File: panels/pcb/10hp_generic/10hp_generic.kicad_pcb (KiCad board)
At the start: 2 copper layers, 49.9 x 109.2 mm, 81 parts, among them J1 Conn_02x04_Odd_Even, J2 SWD, SW1 SW_Push, SW10 SW_Push, SW11 SW_Push, SW12 SW_Push, SW13 SW_Push, SW14 SW_Push, SW15 SW_Push, SW16 SW_Push, SW2 SW_Push, SW3 SW_Push, SW4 SW_Push, SW5 SW_Push, SW6 SW_Push, SW7 SW_Push, SW8 SW_Push, SW9 SW_Push, U1 STM32F072RBTx, U2 AMS1117-3.3

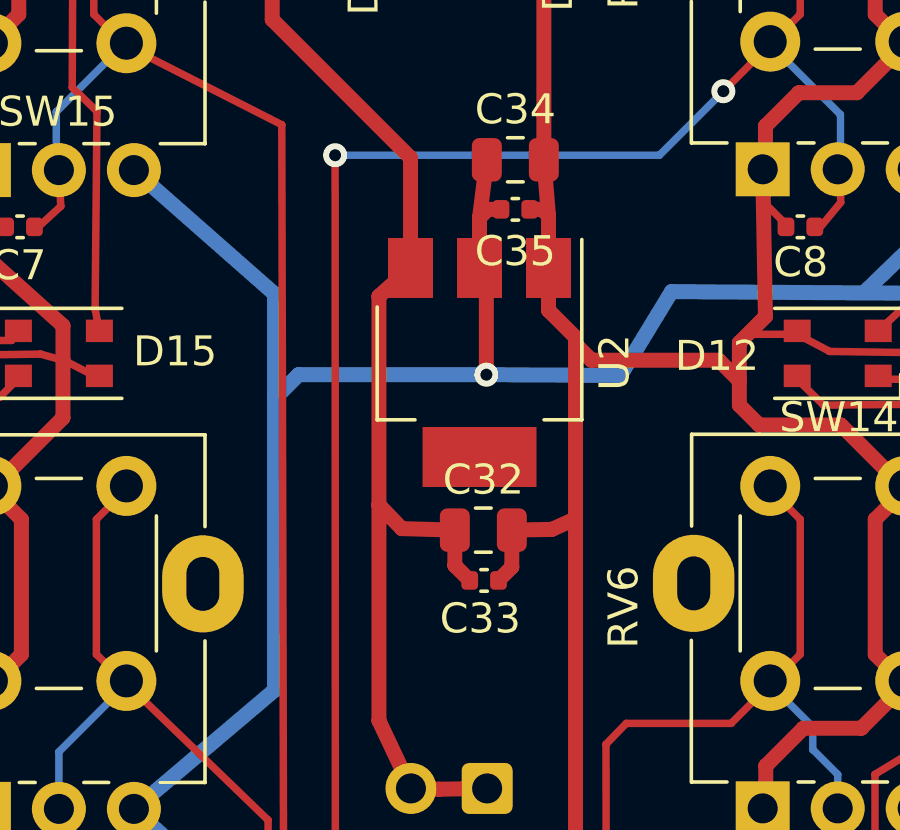
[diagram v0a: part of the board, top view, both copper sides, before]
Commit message: Fixes some component values
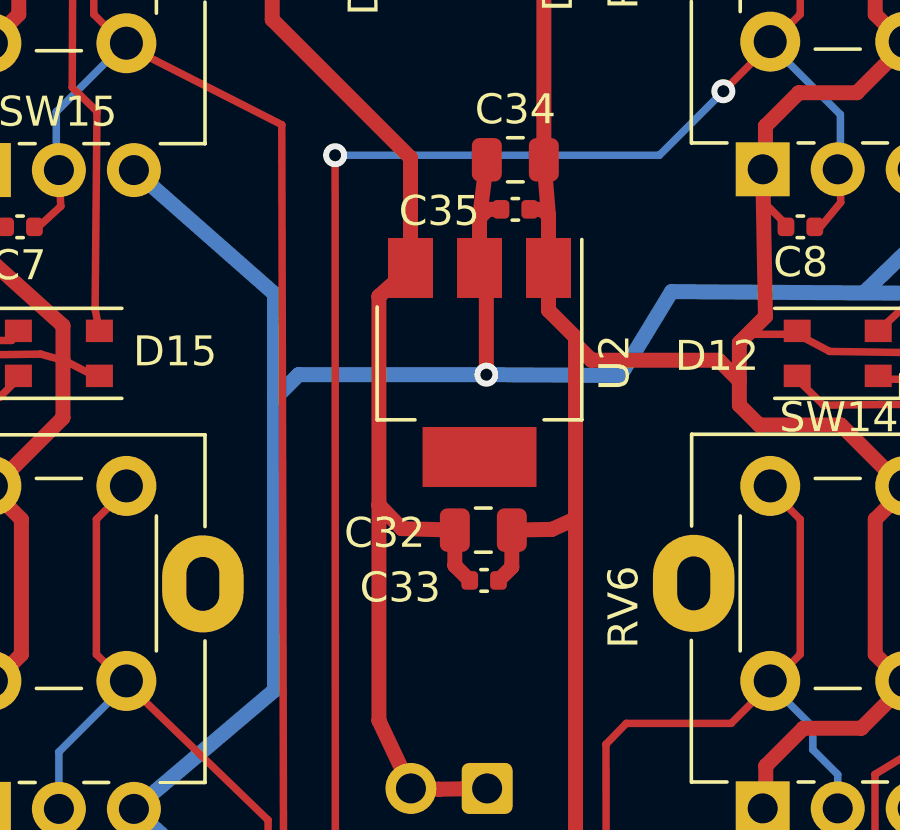
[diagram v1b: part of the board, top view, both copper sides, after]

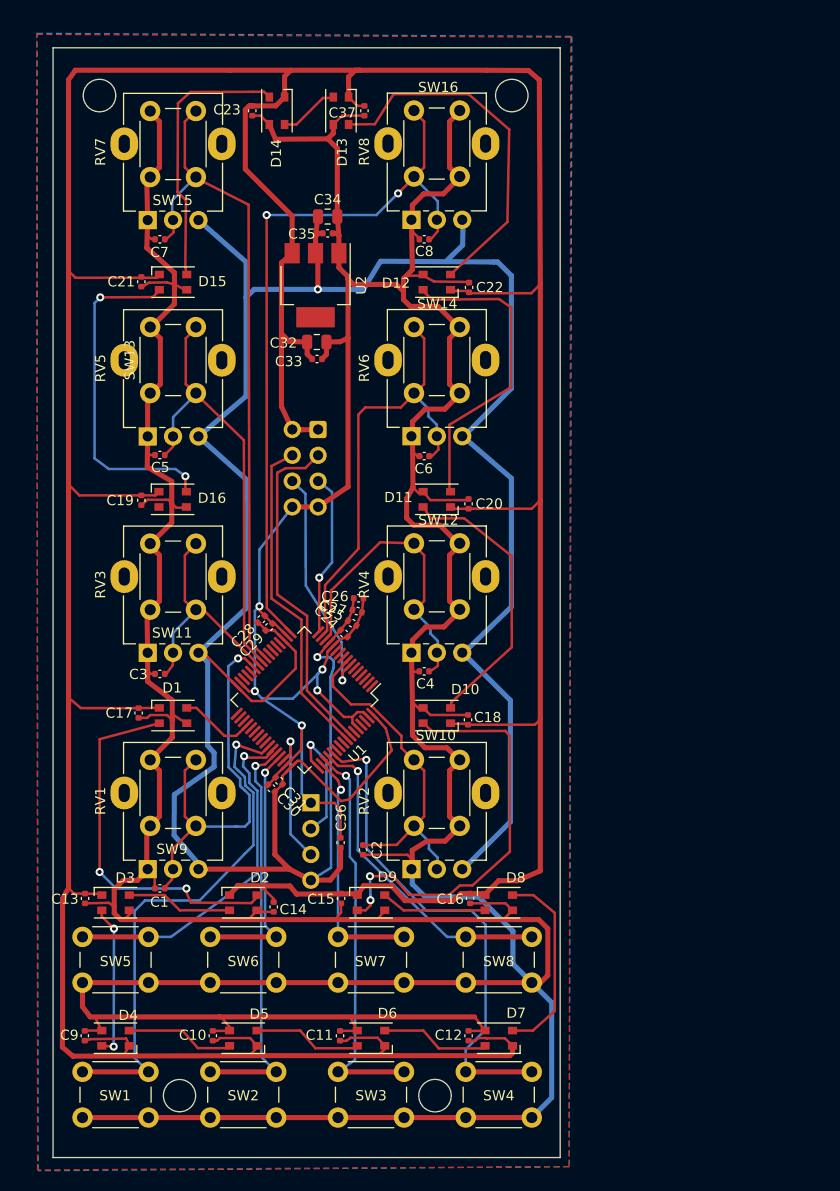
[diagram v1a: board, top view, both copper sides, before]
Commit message: R2 of generic PCB using different components
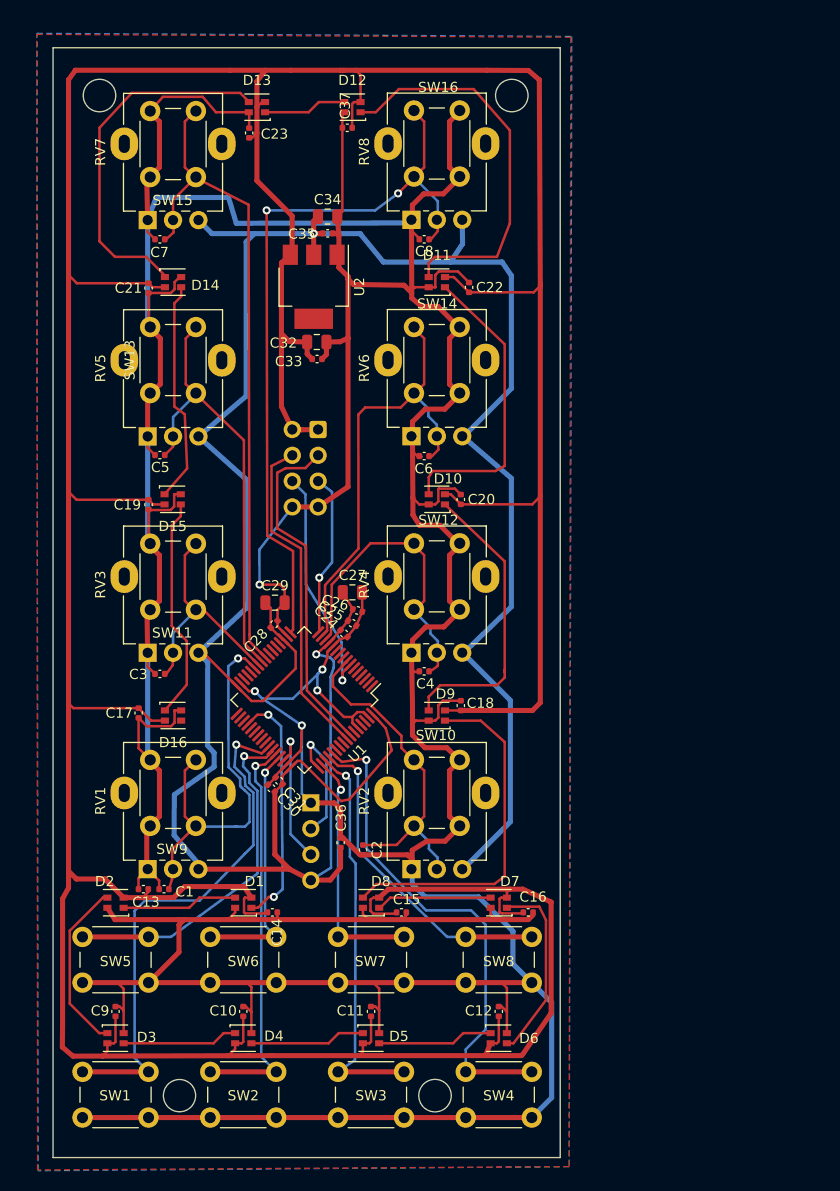
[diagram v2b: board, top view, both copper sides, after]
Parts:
- removed the D1 at (62.6, 108.9)
- removed the D13 at (79.1, 49.4)
- removed the D4 at (56.9, 140.7)
- removed the D7 at (94.7, 140.7)
- added D12: WS2812B, WS2812:XL-2121RGBC-WS2812B, F.Cu at (80.3, 49.0)
- added D15: WS2812B, WS2812:XL-2121RGBC-WS2812B, F.Cu at (62.6, 87.6)
- added D3: WS2812B, WS2812:XL-2121RGBC-WS2812B, F.Cu at (56.9, 140.7)
- added D6: WS2812B, WS2812:XL-2121RGBC-WS2812B, F.Cu at (94.7, 140.7)
- C27, C29: footprint Capacitor_SMD:C_0402_1005Metric -> Capacitor_SMD:C_0805_2012Metric
- D1: renamed from D2; footprint WS2812:XL-3528RGBW-WS2812B -> WS2812:XL-2121RGBC-WS2812B
- D10: renamed from D11; footprint WS2812:XL-3528RGBW-WS2812B -> WS2812:XL-2121RGBC-WS2812B
- D11: renamed from D12; footprint WS2812:XL-3528RGBW-WS2812B -> WS2812:XL-2121RGBC-WS2812B
- D13: renamed from D14; footprint WS2812:XL-3528RGBW-WS2812B -> WS2812:XL-2121RGBC-WS2812B
- D14: renamed from D15; footprint WS2812:XL-3528RGBW-WS2812B -> WS2812:XL-2121RGBC-WS2812B
- D16: footprint WS2812:XL-3528RGBW-WS2812B -> WS2812:XL-2121RGBC-WS2812B
- D2: renamed from D3; footprint WS2812:XL-3528RGBW-WS2812B -> WS2812:XL-2121RGBC-WS2812B
- D4: renamed from D5; footprint WS2812:XL-3528RGBW-WS2812B -> WS2812:XL-2121RGBC-WS2812B
- D5: renamed from D6; footprint WS2812:XL-3528RGBW-WS2812B -> WS2812:XL-2121RGBC-WS2812B
- D7: renamed from D8; footprint WS2812:XL-3528RGBW-WS2812B -> WS2812:XL-2121RGBC-WS2812B
- D8: renamed from D9; footprint WS2812:XL-3528RGBW-WS2812B -> WS2812:XL-2121RGBC-WS2812B
- D9: renamed from D10; footprint WS2812:XL-3528RGBW-WS2812B -> WS2812:XL-2121RGBC-WS2812B
- moved D16 21.3 mm to (62.6, 108.9), turned to 180 degrees
- moved C15 6.10 mm to (85.1, 128.3), turned to 0 degrees
- moved C16 5.88 mm to (97.6, 128.3), turned to 0 degrees
- moved C13 5.81 mm to (59.7, 126.0), turned to 180 degrees
- moved C11 3.88 mm to (82.1, 138.0)
- moved C9 3.86 mm to (56.9, 138.0)
- moved C10 3.84 mm to (69.5, 138.0)
- moved C12 3.82 mm to (94.7, 138.0)
- moved C29 2.46 mm to (72.6, 97.8), turned to 0 degrees
- moved C37 2.38 mm to (79.8, 51.1), turned to 180 degrees
- moved C23 2.21 mm to (70.1, 51.6), turned to 90 degrees
- moved D13 2.00 mm to (70.9, 49.0), turned to 0 degrees
- moved C27 1.90 mm to (80.3, 96.8), turned to 0 degrees
- moved C18 1.57 mm to (90.9, 107.9)
- moved C28 1.35 mm to (72.6, 99.9)
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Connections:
- D1 pad 1: +5V -> GND
- D1 pad 2: Net-(D2-Pad2) -> WS2812
- D1 pad 3: GND -> +5V
- D1 pad 4: Net-(D1-Pad2) -> Net-(D1-Pad4)
- D10 pad 1: +5V -> GND
- D10 pad 2: Net-(D11-Pad2) -> Net-(D10-Pad2)
- D10 pad 3: GND -> +5V
- D10 pad 4: Net-(D10-Pad2) -> Net-(D10-Pad4)
- D11 pad 1: +5V -> GND
- D11 pad 2: Net-(D12-Pad2) -> Net-(D10-Pad4)
- D11 pad 3: GND -> +5V
- D11 pad 4: Net-(D11-Pad2) -> Net-(D11-Pad4)
- D13 pad 1: +5V -> GND
- D13 pad 2: Net-(D14-Pad2) -> Net-(D12-Pad4)
- D13 pad 3: GND -> +5V
- D13 pad 4: Net-(D13-Pad2) -> Net-(D13-Pad4)
- D14 pad 1: +5V -> GND
- D14 pad 2: Net-(D15-Pad2) -> Net-(D13-Pad4)
- D14 pad 3: GND -> +5V
- D14 pad 4: Net-(D14-Pad2) -> Net-(D14-Pad4)
- D16 pad 1: +5V -> GND
- D16 pad 3: GND -> +5V
- D16 pad 4: Net-(D15-Pad2) -> Net-(D16-Pad4)
- D2 pad 1: +5V -> GND
- D2 pad 2: Net-(D3-Pad2) -> Net-(D1-Pad4)
- D2 pad 3: GND -> +5V
- D2 pad 4: Net-(D2-Pad2) -> Net-(D2-Pad4)
- D4 pad 1: +5V -> GND
- D4 pad 2: Net-(D5-Pad2) -> Net-(D3-Pad4)
- D4 pad 3: GND -> +5V
- D4 pad 4: Net-(D4-Pad2) -> Net-(D4-Pad4)
- D5 pad 1: +5V -> GND
- D5 pad 2: Net-(D6-Pad2) -> Net-(D4-Pad4)
- D5 pad 3: GND -> +5V
- D5 pad 4: Net-(D5-Pad2) -> Net-(D5-Pad4)
- D7 pad 1: +5V -> GND
- D7 pad 2: Net-(D8-Pad2) -> Net-(D6-Pad4)
- D7 pad 3: GND -> +5V
- D7 pad 4: Net-(D7-Pad2) -> Net-(D7-Pad4)
- D8 pad 1: +5V -> GND
- D8 pad 2: Net-(D10-Pad4) -> Net-(D7-Pad4)
- D8 pad 3: GND -> +5V
- D8 pad 4: Net-(D8-Pad2) -> Net-(D8-Pad4)
- D9 pad 1: +5V -> GND
- D9 pad 2: Net-(D10-Pad2) -> Net-(D8-Pad4)
- D9 pad 3: GND -> +5V
- D9 pad 4: Net-(D10-Pad4) -> Net-(D10-Pad2)
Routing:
- net Net-(D11-Pad4): track 0.00 -> 38.5 mm
- net Net-(D1-Pad2): track 36.4 -> 0.00 mm, vias 2 -> 0
- net Net-(D13-Pad4): track 0.00 -> 35.7 mm
- net Net-(D12-Pad2): track 35.5 -> 0.00 mm
- net Net-(D8-Pad4): track 0.00 -> 34.7 mm
- net Net-(D15-Pad2): track 33.3 -> 0.00 mm, vias 2 -> 0
- net Net-(D11-Pad2): track 30.9 -> 0.00 mm
- net Net-(D14-Pad2): track 26.8 -> 0.00 mm
- net Net-(D15-Pad4): track 0.00 -> 22.0 mm
- net Net-(D14-Pad4): track 0.00 -> 22.0 mm
- net Net-(D7-Pad2): track 19.3 -> 0.00 mm
- net Net-(D6-Pad4): track 0.00 -> 18.6 mm
- net Net-(D2-Pad4): track 0.00 -> 17.1 mm
- net WS2812: track 7.66 -> 24.0 mm, vias 0 -> 2
- net Net-(D3-Pad2): track 15.1 -> 0.00 mm, vias 2 -> 0
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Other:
- board text added: "Generic Modular Panel 14HP - Rev 2"
- board text removed: "Generic Modular Panel 14HP - Rev 1"

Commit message: More website stuff
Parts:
- removed the C37 at (79.8, 51.1)
- added C24: 100nF, Capacitor_SMD:C_0402_1005Metric, F.Cu at (79.8, 51.1)
- renumbered C24 to C37
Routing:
- removed copper zone on F.Cu, net GND
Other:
- board text added: "+5V"

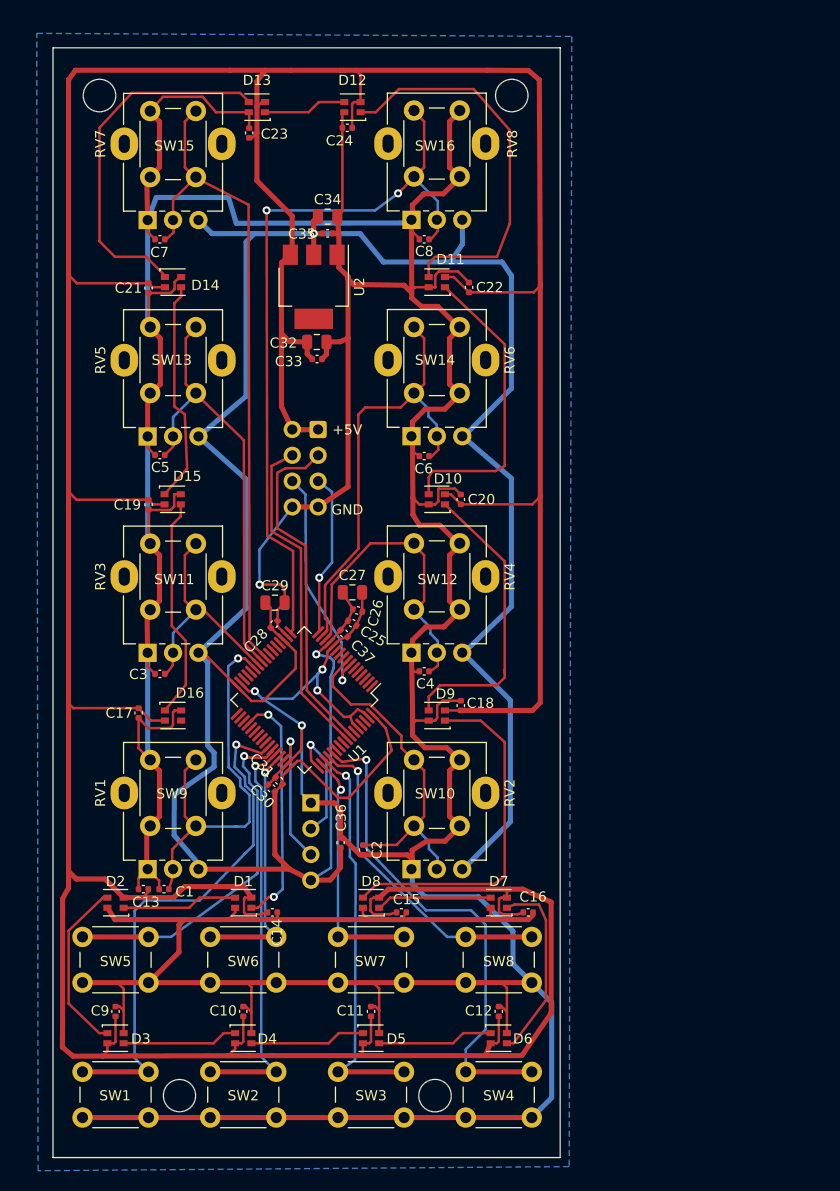
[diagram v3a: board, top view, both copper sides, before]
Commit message: Improvements to generic 10HP board layout. Implement exponential moving average filter on ADC reads.
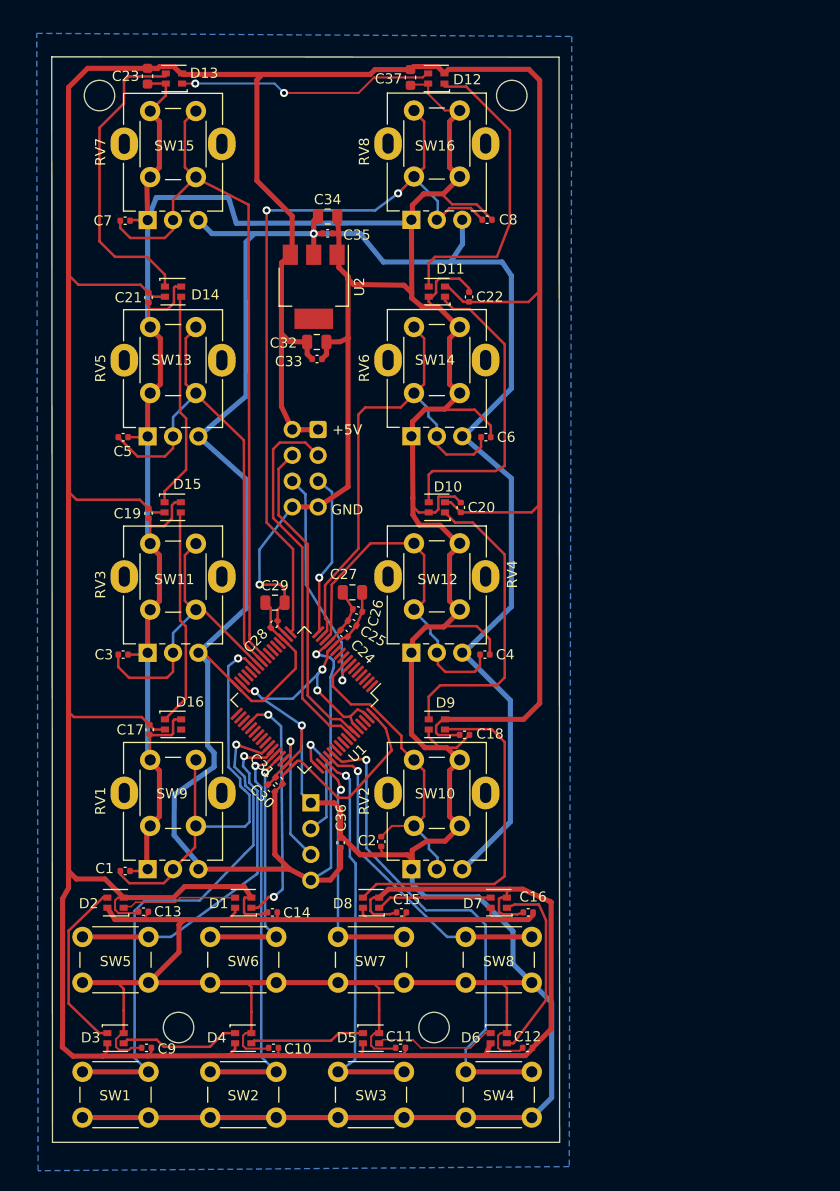
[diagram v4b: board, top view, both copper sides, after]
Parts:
- C23: footprint Capacitor_SMD:C_0402_1005Metric -> Capacitor_SMD:C_0603_1608Metric
- C37: renamed from C24; footprint Capacitor_SMD:C_0402_1005Metric -> Capacitor_SMD:C_0603_1608Metric
- RV1, RV2, RV3, RV4, RV5, RV6, RV7, RV8: footprint Potentiometer_THT:Potentiometer_Alpha_RD901F-40-00D_Single_Vertical -> riban:Potentiometer_9mm_Vertical
- moved C23 11.5 mm to (60.1, 46.0), turned to -90 degrees
- moved D12 8.72 mm to (88.5, 46.2)
- moved D13 8.64 mm to (62.7, 46.2)
- moved C37 7.95 mm to (86.0, 46.1), turned to -90 degrees
- moved C8 6.49 mm to (93.5, 60.1), turned to 180 degrees
- moved C6 6.35 mm to (93.4, 81.5), turned to 180 degrees
- moved C4 6.20 mm to (93.3, 102.9), turned to 180 degrees
- moved C9 4.70 mm to (60.0, 141.6), turned to 180 degrees
- moved C10 4.66 mm to (72.5, 141.6), turned to 180 degrees
- moved C11 4.61 mm to (85.0, 141.6), turned to 180 degrees
- moved C12 4.57 mm to (97.5, 141.6), turned to 180 degrees
- moved C1 4.22 mm to (57.9, 124.2), turned to 0 degrees
- moved C3 4.08 mm to (57.7, 102.9), turned to 180 degrees
- moved C5 4.02 mm to (57.7, 81.5), turned to 180 degrees
- moved C7 3.87 mm to (57.9, 60.2), turned to 180 degrees
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- renumbered C37 to C24
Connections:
- D16 pad 4: Net-(D16-Pad4) -> unconnected-(D16-Pad4)
- J1 pad 3: SDA -> SCL
- J1 pad 4: SCL -> SDA
- U1 pad 1: Net-(U1-Pad1) -> unconnected-(U1-Pad1)
- U1 pad 10: Net-(U1-Pad10) -> unconnected-(U1-Pad10)
- U1 pad 11: Net-(U1-Pad11) -> unconnected-(U1-Pad11)
- U1 pad 2: Net-(U1-Pad2) -> unconnected-(U1-Pad2)
- U1 pad 20: Net-(U1-Pad20) -> unconnected-(U1-Pad20)
- U1 pad 21: Net-(U1-Pad21) -> unconnected-(U1-Pad21)
- U1 pad 22: Net-(U1-Pad22) -> unconnected-(U1-Pad22)
- U1 pad 23: Net-(U1-Pad23) -> unconnected-(U1-Pad23)
- U1 pad 28: Net-(U1-Pad28) -> unconnected-(U1-Pad28)
- U1 pad 29: Net-(U1-Pad29) -> unconnected-(U1-Pad29)
- U1 pad 3: Net-(U1-Pad3) -> unconnected-(U1-Pad3)
- U1 pad 30: Net-(U1-Pad30) -> unconnected-(U1-Pad30)
- U1 pad 33: Net-(U1-Pad33) -> unconnected-(U1-Pad33)
- U1 pad 34: Net-(U1-Pad34) -> unconnected-(U1-Pad34)
- U1 pad 35: Net-(U1-Pad35) -> unconnected-(U1-Pad35)
- U1 pad 37: Net-(U1-Pad37) -> unconnected-(U1-Pad37)
- U1 pad 38: Net-(U1-Pad38) -> unconnected-(U1-Pad38)
- U1 pad 39: Net-(U1-Pad39) -> unconnected-(U1-Pad39)
- U1 pad 4: Net-(U1-Pad4) -> unconnected-(U1-Pad4)
- U1 pad 40: Net-(U1-Pad40) -> unconnected-(U1-Pad40)
- U1 pad 41: Net-(U1-Pad41) -> unconnected-(U1-Pad41)
- U1 pad 5: Net-(U1-Pad5) -> unconnected-(U1-Pad5)
- U1 pad 54: Net-(U1-Pad54) -> unconnected-(U1-Pad54)
- U1 pad 55: Net-(U1-Pad55) -> unconnected-(U1-Pad55)
- U1 pad 56: Net-(U1-Pad56) -> unconnected-(U1-Pad56)
- U1 pad 57: SCL -> unconnected-(U1-Pad57)
- U1 pad 58: SDA -> SCL
- U1 pad 59: Net-(U1-Pad59) -> SDA
- U1 pad 6: Net-(U1-Pad6) -> unconnected-(U1-Pad6)
- U1 pad 61: Net-(U1-Pad61) -> unconnected-(U1-Pad61)
- U1 pad 62: Net-(U1-Pad62) -> unconnected-(U1-Pad62)
- U1 pad 9: Net-(U1-Pad9) -> unconnected-(U1-Pad9)
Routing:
- net Net-(D12-Pad4): track 8.21 -> 25.4 mm, vias 0 -> 2
- net +5V: track 453.5 -> 442.1 mm
- net Net-(D11-Pad4): track 38.5 -> 30.2 mm
- net POT3: track 23.0 -> 29.9 mm
- net Net-(D13-Pad4): track 35.7 -> 30.0 mm
- net POT5: track 43.6 -> 49.1 mm
- net POT7: track 66.3 -> 71.2 mm
- net GND: track 626.2 -> 631.1 mm
- net POT4: track 30.2 -> 34.9 mm
- net POT6: track 44.3 -> 48.9 mm
- net SCL: track 32.7 -> 37.2 mm
- net POT1: track 39.6 -> 43.3 mm
- net POT8: track 73.5 -> 76.2 mm
- net POT2: track 33.5 -> 30.9 mm
- net SDA: track 33.8 -> 31.4 mm
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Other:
- board size 49.9 x 109.2 mm -> 50 x 106.8 mm
- net class Default removed
- board text added: "Generic Modular Panel 10HP - Rev 2"
- board text removed: "Generic Modular Panel 14HP - Rev 2"
